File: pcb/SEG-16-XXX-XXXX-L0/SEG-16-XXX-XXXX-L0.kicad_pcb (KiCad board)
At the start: 2 copper layers, 66.7 x 100 mm, 191 parts, among them J1 0472861001, J2 0472861001, J3 DTA_FLOW_LEFT, J4 DATA_FLOW_RIGHT, U1 STM8S003, U2 TM1640

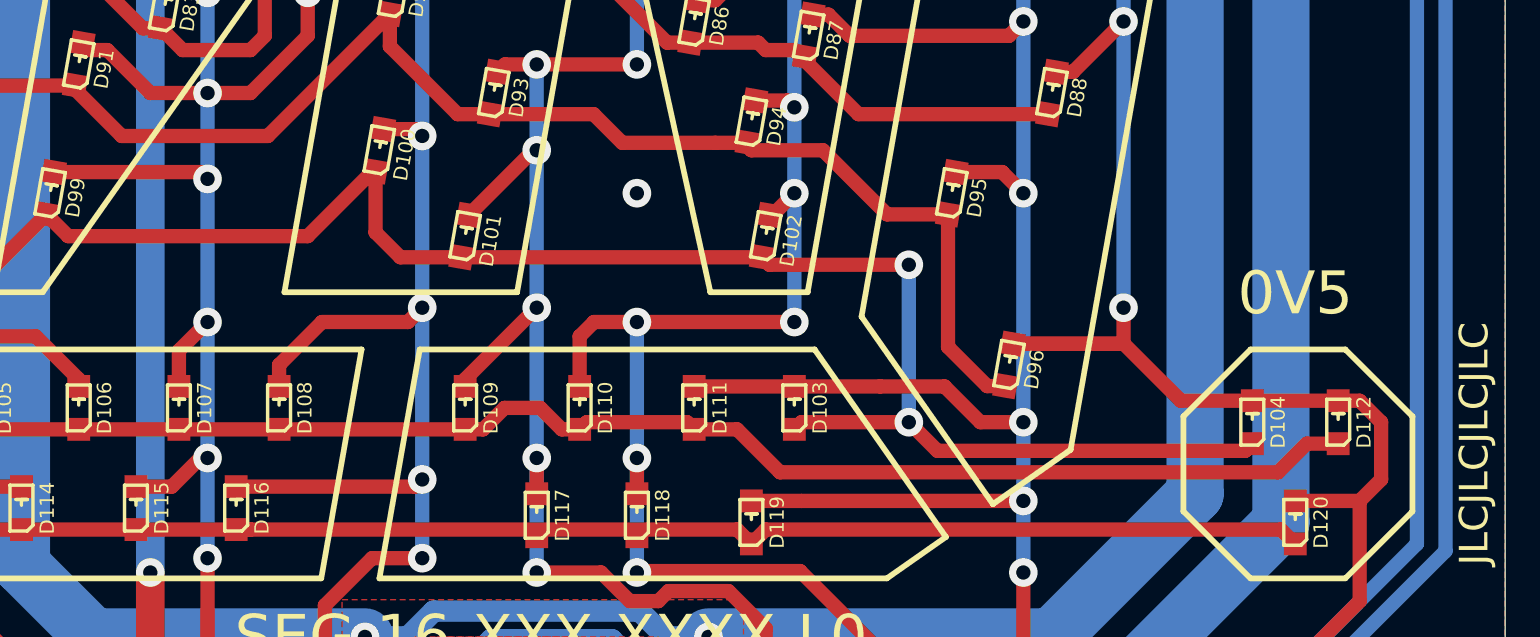
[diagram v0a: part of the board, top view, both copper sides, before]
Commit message: Updated to 0V6 changed images
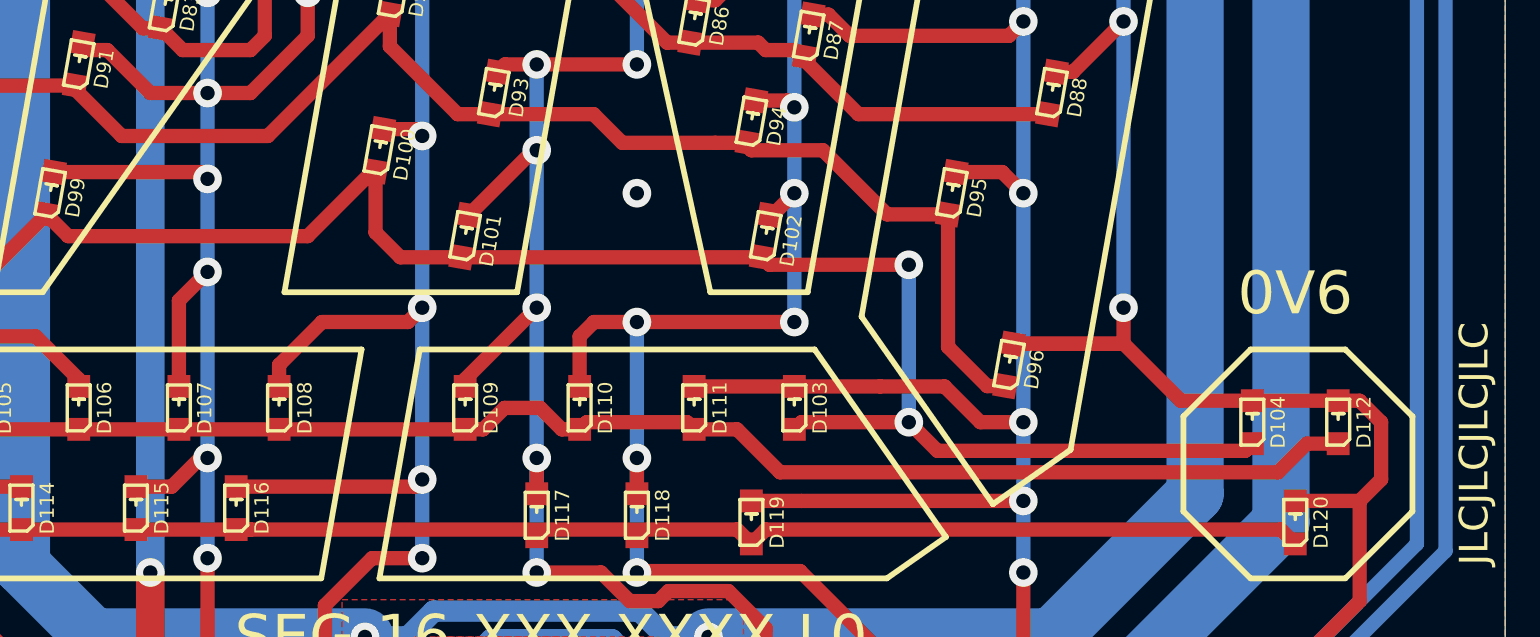
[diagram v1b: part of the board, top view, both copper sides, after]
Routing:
- net /SEG3: track 209.2 -> 210.9 mm
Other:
- board text added: "0V6"
- board text removed: "0V5"
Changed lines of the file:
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@@
     )
   )
-  (gr_text 0V5 (at 26 30) (layer F.SilkS)
+  (gr_text 0V6 (at 26 30) (layer F.SilkS)
     (effects (font (size 1.5 1.5) (thickness 0.3)))
   )
@@
   (segment (start -12.238606 19.261394) (end -12 19.5) (width 0.5) (layer F.Cu) (net 6))
   (segment (start -12 19.5) (end -12 23) (width 0.5) (layer B.Cu) (net 6))
-  (via (at -12 31) (size 1) (drill 0.5) (layers F.Cu B.Cu) (net 6))
-  (segment (start -13 32) (end -12 31) (width 0.5) (layer F.Cu) (net 6))
-  (segment (start -13 33.25) (end -13 32) (width 0.5) (layer F.Cu) (net 6))
-  (segment (start -12 31) (end -12 26) (width 0.5) (layer B.Cu) (net 6))
   (via (at -0.5 -6.25) (size 1) (drill 0.5) (layers F.Cu B.Cu) (net 6))
   (segment (start -0.5 4.5) (end -0.5 -6.25) (width 0.5) (layer B.Cu) (net 6))
@@
   (segment (start -0.5 -6.25) (end -3.25 -6.25) (width 0.5) (layer F.Cu) (net 6))
   (via (at -12 35.75) (size 1) (drill 0.5) (layers F.Cu B.Cu) (net 6))
-  (segment (start -12 35.75) (end -12 31) (width 0.5) (layer B.Cu) (net 6))
   (segment (start -13.25 36.75) (end -14.5 36.75) (width 0.5) (layer F.Cu) (net 6))
   (segment (start -12.25 35.75) (end -13.25 36.75) (width 0.5) (layer F.Cu) (net 6))
@@
   (segment (start -7 -28) (end -7.869764 -27.130236) (width 0.5) (layer F.Cu) (net 6))
   (via (at -0.5 -29.25) (size 1) (drill 0.5) (layers F.Cu B.Cu) (net 6))
+  (via (at -12 29.25) (size 1) (drill 0.5) (layers F.Cu B.Cu) (net 6))
+  (segment (start -13 30.25) (end -13 33.25) (width 0.5) (layer F.Cu) (net 6))
+  (segment (start -12 29.25) (end -13 30.25) (width 0.5) (layer F.Cu) (net 6))
+  (segment (start -12 29.25) (end -12 26) (width 0.5) (layer B.Cu) (net 6))
+  (segment (start -12 35.75) (end -12 29.25) (width 0.5) (layer B.Cu) (net 6))
   (via (at 3 -36) (size 1) (drill 0.5) (layers F.Cu B.Cu) (net 7))
   (segment (start 3 -34.75) (end 3 -36) (width 0.5) (layer F.Cu) (net 7))

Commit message: Added WDT to display code
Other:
- net class Default removed

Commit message: Reverted version to kicad 5.x, fixed OSHW Marking, added better led markings and legend
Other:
- net class Default added: clearance 0.127, trace_width 0.127, via_dia 0.45, via_drill 0.3
- board text added: "+"
- board text added: "-"
- board text added: "0603 LED"
- board text added: "2 Layer 1.0mm FR4 1oz White Silk Green Mask E-Test Required 1.152mm Tooling Holes 1.5mmx3mm Fiducials"
- board text added: "A"
- board text added: "Dot"
- board text added: "K"
- board text removed: "2 Layer 1.0mm FR4 1oz White SIlk Green Mask E-Test Required 1.152mm Tooling Holes 1.5mmx3mm Fiducials"
